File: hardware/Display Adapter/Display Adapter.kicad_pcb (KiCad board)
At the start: 2 copper layers, 38.1 x 38.1 mm, 2 parts, among them J1 IDC-Header_2x07_P2.54mm, J2 ILI9341 2.8" touch TFT

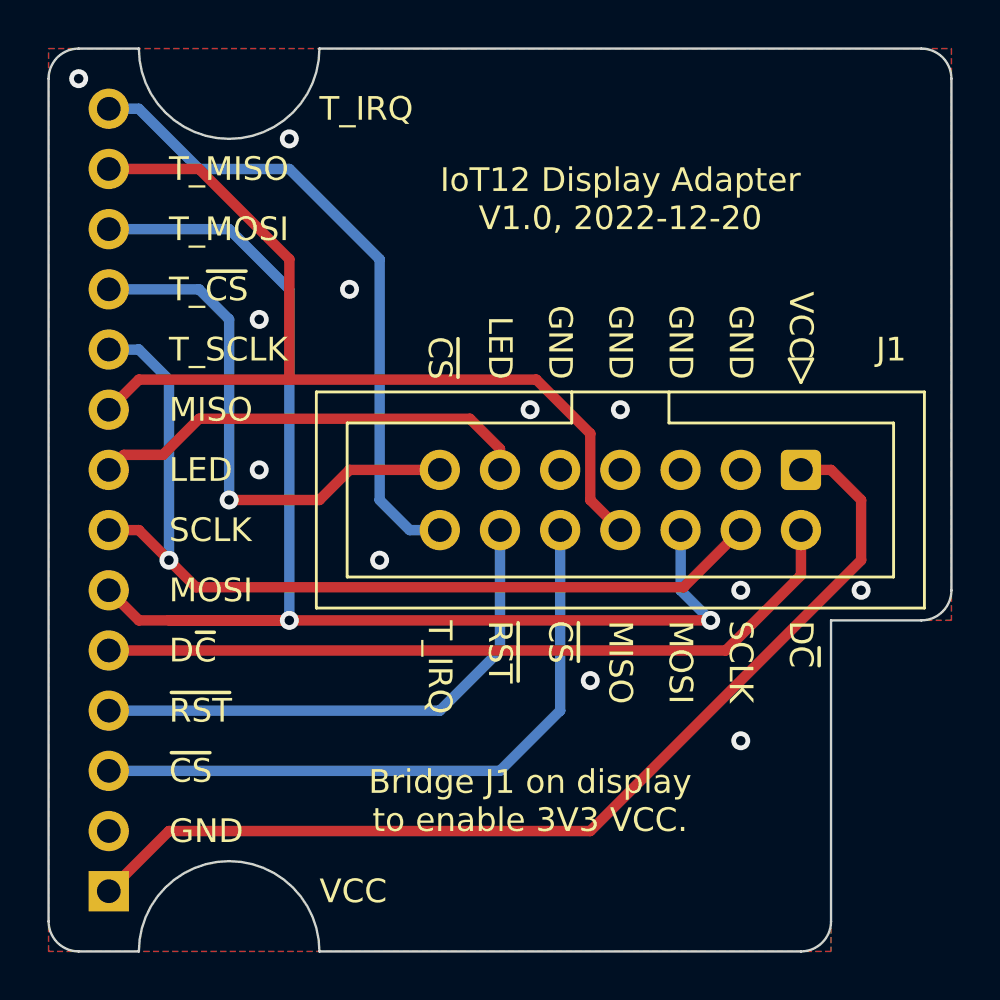
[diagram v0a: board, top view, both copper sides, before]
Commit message: Update Display Adapter project to Kicad 7.0.2
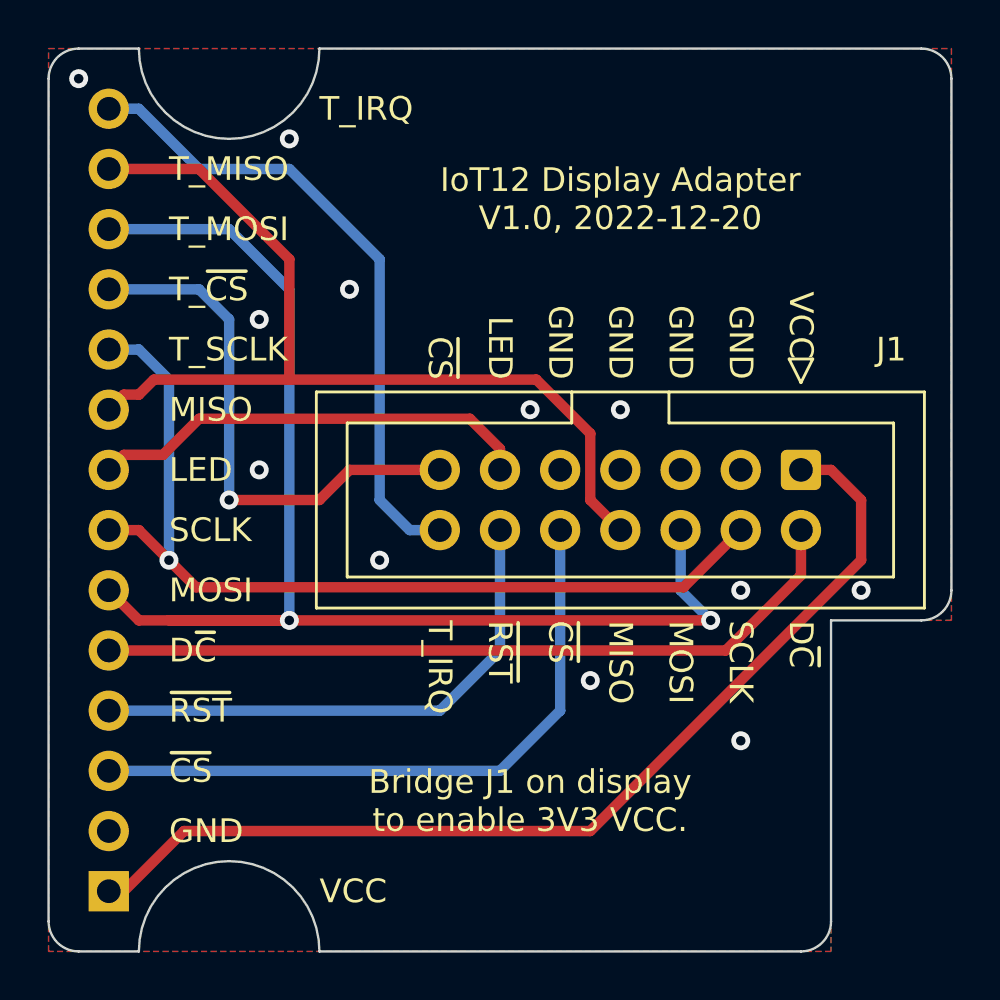
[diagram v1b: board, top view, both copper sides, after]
